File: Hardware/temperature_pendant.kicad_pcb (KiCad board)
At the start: 2 copper layers, 38.1 x 25.4 mm, 5 parts, among them J1 CONN-6, SW1 SW-MOM, U1 BLINKM/MINM, U2 TMP3X

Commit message: Updated board
Updated board and first revision routing
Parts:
- SW1: footprint SW_FSM4JSMATR -> SW-EVQP7
- moved BT1 44.7 mm to (221.0, 119.4), turned to 0 degrees
- moved U2 28.1 mm to (222.2, 146.1)
- moved SW1 5.24 mm to (221.0, 134.6)
- moved J1 1.27 mm to (208.3, 129.5)
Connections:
- J1 pad 1: (no net) -> RST
- J1 pad 2: (no net) -> GND
- J1 pad 3: (no net) -> +BATT
- J1 pad 4: (no net) -> SW
- J1 pad 5: (no net) -> TEMP
- J1 pad 6: (no net) -> MISO
- SW1 pad 1: (no net) -> SW
- SW1 pad 2: (no net) -> +BATT
- U1 pad 1: (no net) -> RST
- U1 pad 2: (no net) -> GND
- U1 pad 3: (no net) -> +BATT
- U1 pad 4: (no net) -> SW
- U1 pad 5: (no net) -> TEMP
- U1 pad 6: (no net) -> MISO
- U2 pad 1: (no net) -> +BATT
- U2 pad 2: (no net) -> TEMP
- U2 pad 3: (no net) -> GND
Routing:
- net +BATT: track 0.00 -> 53.2 mm
- net SW: track 0.00 -> 34.8 mm
- net TEMP: track 0.00 -> 28.0 mm
- net RST: track 0.00 -> 18.0 mm
- net MISO: track 0.00 -> 18.0 mm
- added copper zone on B.Cu, net GND
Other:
- board size 38.1 x 25.4 mm -> 26.7 x 24.1 mm
- board text added: "Matthew Nelson 2013"
- board text added: "Temp Pendant r1"

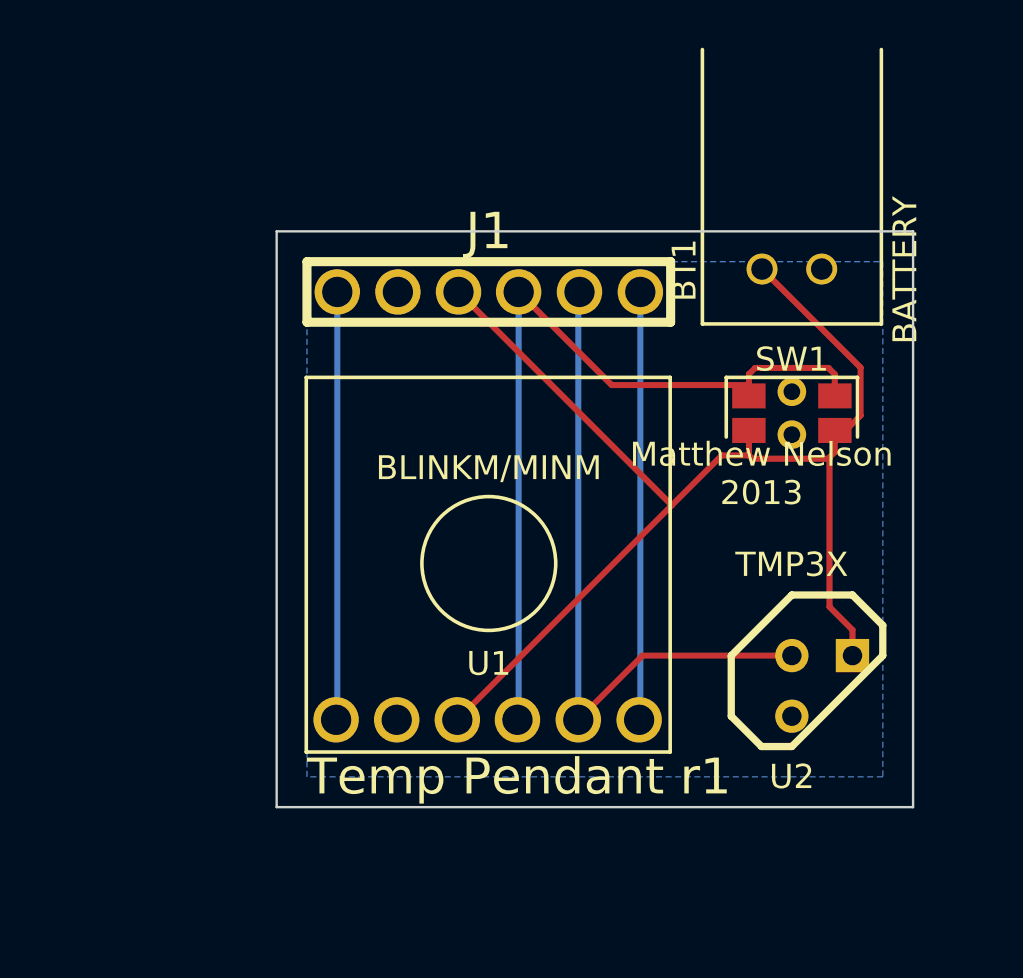
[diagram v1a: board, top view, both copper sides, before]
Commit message: Updated board files for MinM
Updated boards and gerber files for the MinM module instead of the
BlinkM module.  This does result in a smaller size board, slightly.
Otherwise the schematic is the same.
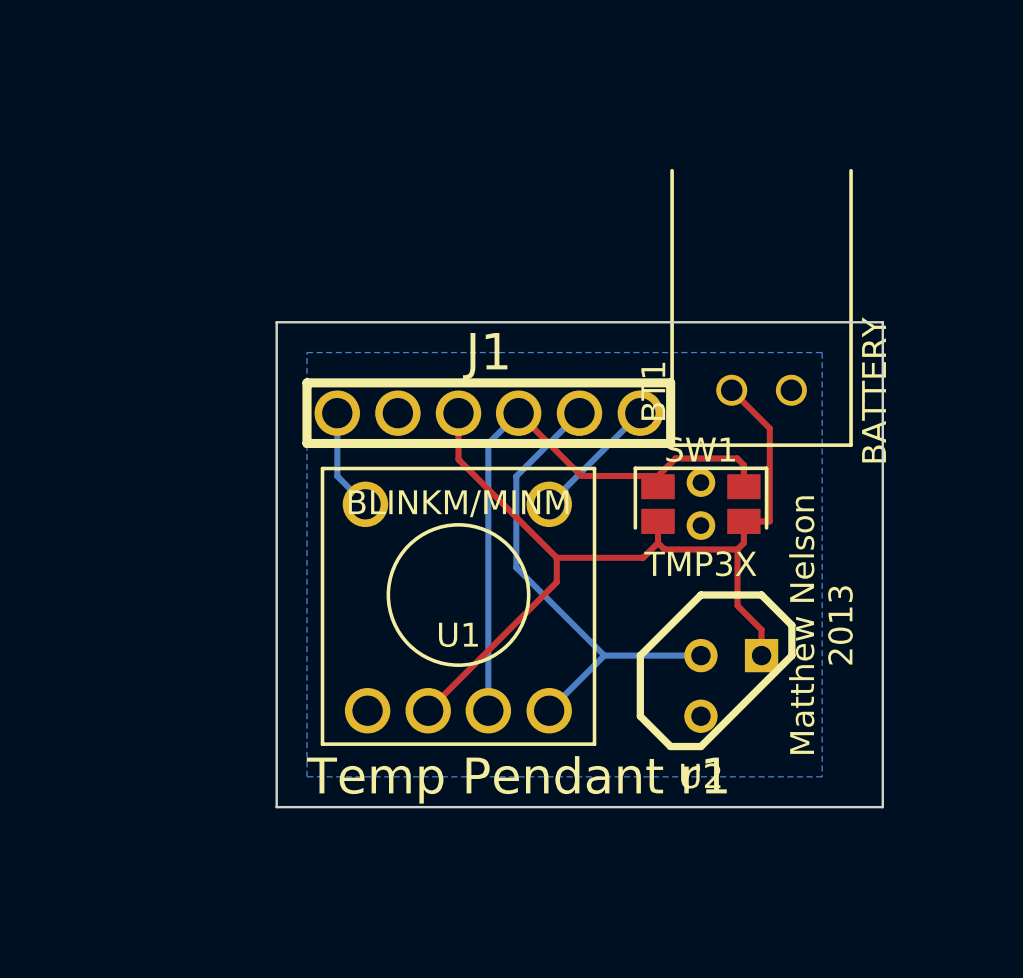
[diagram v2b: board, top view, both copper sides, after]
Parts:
- U1: footprint BlinkM -> MinM
- moved SW1 5.39 mm to (217.2, 138.4)
- moved BT1 5.24 mm to (219.7, 124.5)
- moved J1 5.08 mm to (208.3, 134.6)
- moved U2 3.81 mm to (218.4, 146.1)
- moved U1 1.80 mm to (207.0, 142.2)
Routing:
- net +BATT: track 53.2 -> 38.6 mm
- net RST: track 18.0 -> 4.31 mm
- net MISO: track 18.0 -> 5.40 mm
- net SW: track 34.8 -> 25.3 mm
- net TEMP: track 28.0 -> 20.1 mm
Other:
- board size 26.7 x 24.1 mm -> 25.4 x 20.3 mm
